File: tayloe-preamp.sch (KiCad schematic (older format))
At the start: 13 parts, among them J1 PCB_SMA_EDGE, J2 PCB_SMA_EDGE, J3 Conn_01x01_Female, Q1 2N2222, T1 T37_XFRM

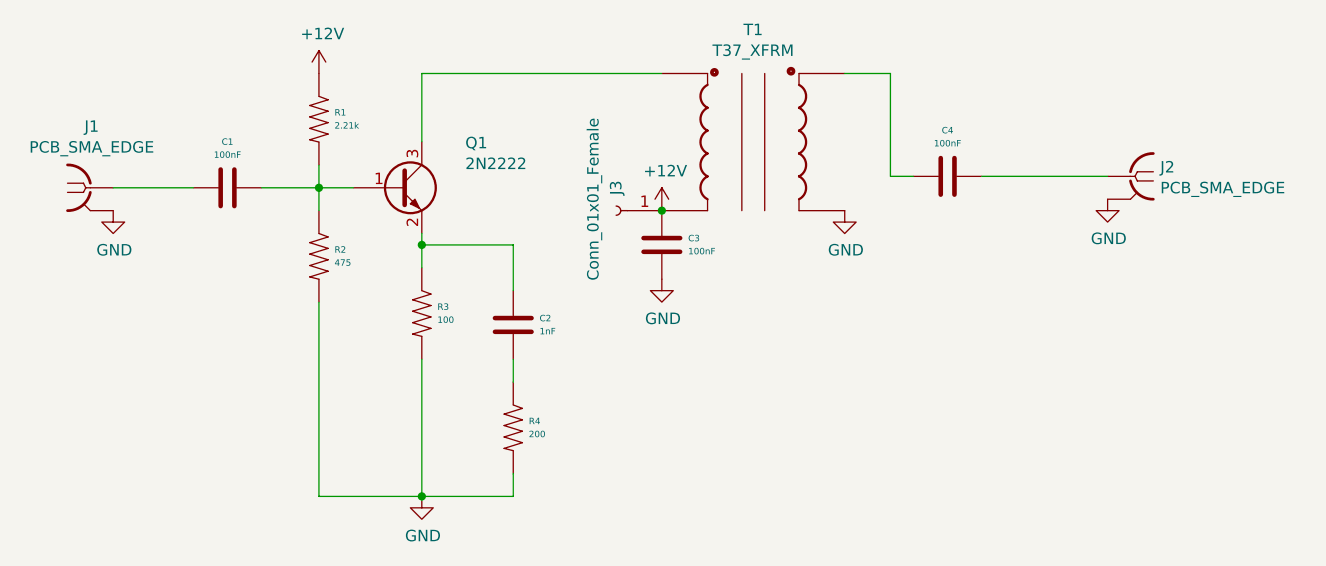
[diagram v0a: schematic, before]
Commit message: added 50 ohm input
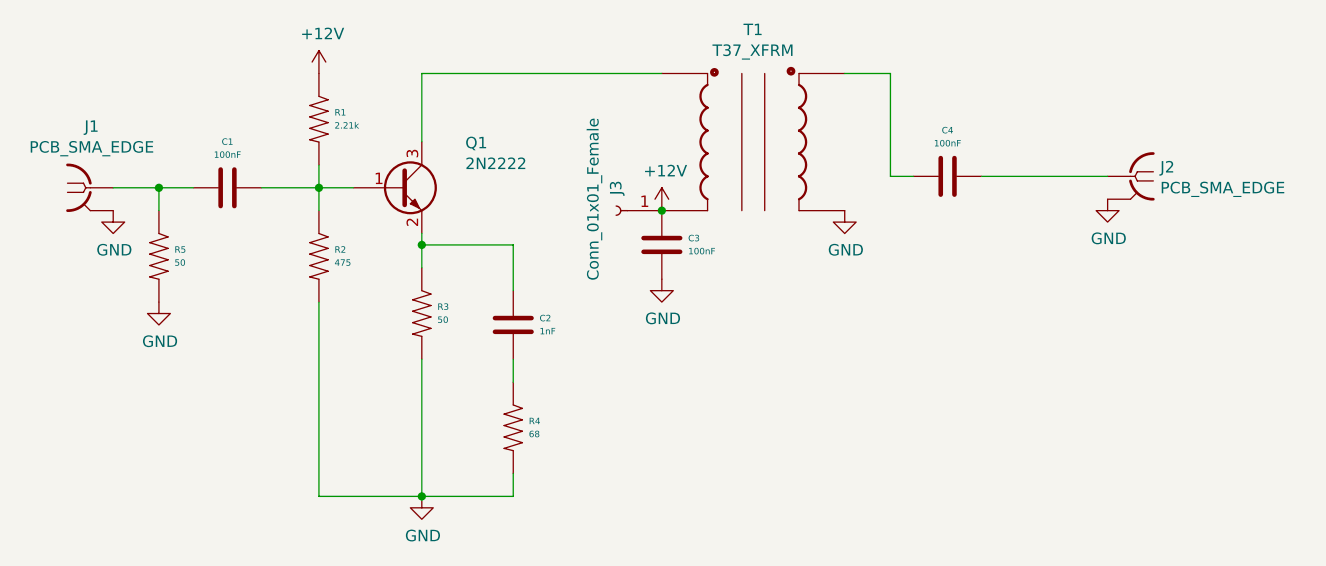
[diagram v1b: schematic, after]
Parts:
- added R5: 50, Xenir:Resistor 1206, symbol Xenir:Resistor
- R3: value 100 -> 50
- R4: value 200 -> 68
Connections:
- net GND: now also R5.2
- net at C1.2, J1.1: now also R5.1
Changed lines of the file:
@@
 P 4050 3750
 F 0 "R3" V 4021 3818 28  0000 L CNN
-F 1 "100" V 4078 3818 28  0000 L CNN
+F 1 "50" V 4078 3818 28  0000 L CNN
 F 2 "Xenir:Resistor 1206" H 4050 3650 50  0001 C CNN
 F 3 "" H 4050 3650 50  0001 C CNN
@@
 P 4450 4250
 F 0 "R4" V 4421 4318 28  0000 L CNN
-F 1 "200" V 4478 4318 28  0000 L CNN
+F 1 "68" V 4478 4318 28  0000 L CNN
 F 2 "Xenir:Resistor 1206" H 4450 4150 50  0001 C CNN
 F 3 "" H 4450 4150 50  0001 C CNN
@@
 $EndComp
 Wire Wire Line
-	2700 3200 3050 3200
+	2700 3200 2900 3200
 Wire Wire Line
 	3350 3200 3600 3200
@@
 	-1   0    0    1
 $EndComp
+$Comp
+L Xenir:Resistor R5
+U 1 1 639CE399
+P 2900 3500
+F 0 "R5" V 2871 3568 28  0000 L CNN
+F 1 "50" V 2928 3568 28  0000 L CNN
+F 2 "Xenir:Resistor 1206" H 2900 3400 50  0001 C CNN
+F 3 "" H 2900 3400 50  0001 C CNN
+	1    2900 3500
+	0    1    1    0
+$EndComp
+$Comp
+L power:GND #PWR0108
+U 1 1 639CEF49
+P 2900 3700
+F 0 "#PWR0108" H 2900 3450 50  0001 C CNN
+F 1 "GND" H 2905 3527 50  0000 C CNN
+F 2 "" H 2900 3700 50  0001 C CNN
+F 3 "" H 2900 3700 50  0001 C CNN
+	1    2900 3700
+	1    0    0    -1
+$EndComp
+Wire Wire Line
+	2900 3300 2900 3200
+Connection ~ 2900 3200
+Wire Wire Line
+	2900 3200 3050 3200
 $EndSCHEMATC

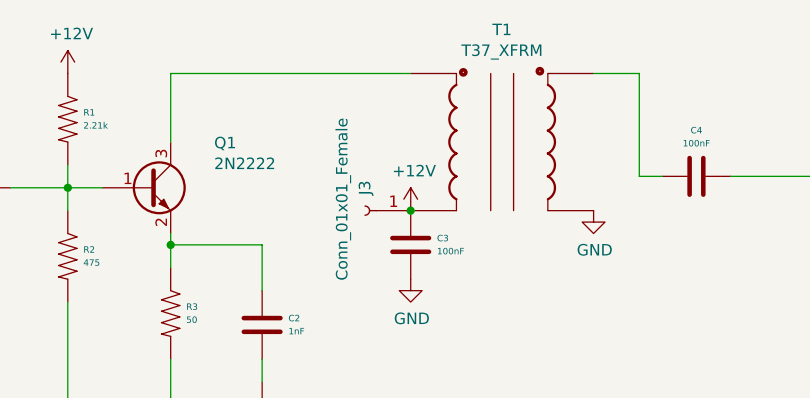
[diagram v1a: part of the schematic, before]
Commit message: changed to inductor
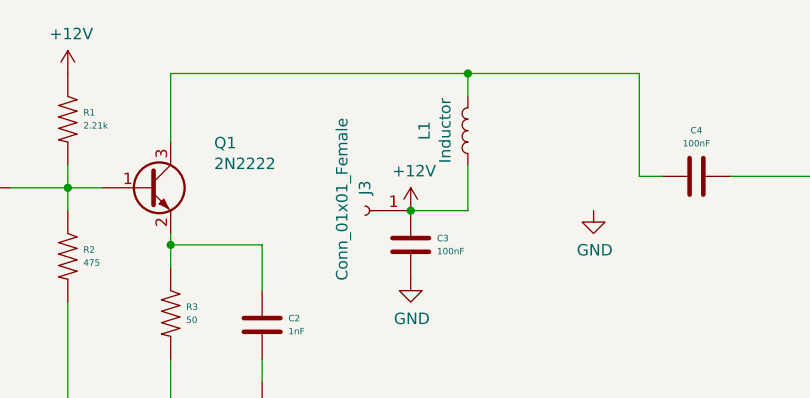
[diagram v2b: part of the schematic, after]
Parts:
- removed T1: T37_XFRM, Xenir:T37 Transformer, symbol Xenir:T37_XFRM
- added L1: Inductor, Xenir:T37_Inductor, symbol Xenir:Inductor
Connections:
- net +12V: now also L1.1
- net at Q1.3 (C): now also C4.2, L1.2
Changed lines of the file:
@@
-$EndComp
-$Comp
-L Xenir:T37_XFRM T1
-U 1 1 639E1E90
-P 5500 2550
-F 0 "T1" H 5500 2591 50  0000 C CNN
-F 1 "T37_XFRM" H 5500 2500 50  0000 C CNN
-F 2 "Xenir:T37 Transformer" H 5500 2550 50  0001 C CNN
-F 3 "" H 5500 2550 50  0001 C CNN
-	1    5500 2550
-	1    0    0    -1
 $EndComp
 $Comp
@@
 	1    0    0    -1
 $EndComp
-Wire Wire Line
-	5900 2700 6100 2700
-Wire Wire Line
-	4050 2700 5100 2700
 Wire Wire Line
 	4050 2700 4050 3000
@@
 Wire Wire Line
 	2900 3200 3050 3200
+$Comp
+L Xenir:Inductor L1
+U 1 1 639CFD79
+P 5350 2950
+F 0 "L1" H 5350 3140 50  0000 C CNN
+F 1 "Inductor" H 5350 3049 50  0000 C CNN
+F 2 "Xenir:T37_Inductor" H 5350 3050 50  0001 C CNN
+F 3 "" H 5350 3050 50  0001 C CNN
+	1    5350 2950
+	0    -1   -1   0
+$EndComp
+Wire Wire Line
+	5350 2700 5350 2800
+Wire Wire Line
+	5350 2700 6100 2700
+Wire Wire Line
+	5350 2700 4050 2700
+Connection ~ 5350 2700
+Wire Wire Line
+	5350 3100 5350 3300
+Wire Wire Line
+	5350 3300 5100 3300
 $EndSCHEMATC

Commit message: gg
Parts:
- L1: value Inductor -> T37-43 10T
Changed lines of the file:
@@
 P 5350 2950
 F 0 "L1" H 5350 3140 50  0000 C CNN
-F 1 "Inductor" H 5350 3049 50  0000 C CNN
+F 1 "T37-43 10T" H 5350 3049 50  0000 C CNN
 F 2 "Xenir:T37_Inductor" H 5350 3050 50  0001 C CNN
 F 3 "" H 5350 3050 50  0001 C CNN

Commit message: gg
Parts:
- C1, C2, C3, C4: symbol Xenir:Capacitor -> tayloe-preamp-rescue:Capacitor-Xenir
- J1, J2: symbol Xenir:PCB_SMA_EDGE -> tayloe-preamp-rescue:PCB_SMA_EDGE-Xenir
- L1: symbol Xenir:Inductor -> tayloe-preamp-rescue:Inductor-Xenir
- Q1: symbol Xenir:2N3904-SMD -> tayloe-preamp-rescue:2N3904-SMD-Xenir
- R1, R2, R3, R4, R5: symbol Xenir:Resistor -> tayloe-preamp-rescue:Resistor-Xenir
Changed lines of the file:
@@
 $EndDescr
 $Comp
-L Xenir:2N3904-SMD Q1
+L tayloe-preamp-rescue:2N3904-SMD-Xenir Q1
 U 1 1 639CC4F8
 P 4050 3050
@@
 $EndComp
 $Comp
-L Xenir:Resistor R1
+L tayloe-preamp-rescue:Resistor-Xenir R1
 U 1 1 639CCA36
 P 3600 2900
@@
 $EndComp
 $Comp
-L Xenir:Resistor R2
+L tayloe-preamp-rescue:Resistor-Xenir R2
 U 1 1 639CD051
 P 3600 3500
@@
 $EndComp
 $Comp
-L Xenir:Resistor R3
+L tayloe-preamp-rescue:Resistor-Xenir R3
 U 1 1 639CD583
 P 4050 3750
@@
 $EndComp
 $Comp
-L Xenir:Resistor R4
+L tayloe-preamp-rescue:Resistor-Xenir R4
 U 1 1 639CD8F7
 P 4450 4250
@@
 $EndComp
 $Comp
-L Xenir:Capacitor C2
+L tayloe-preamp-rescue:Capacitor-Xenir C2
 U 1 1 639CDDE4
 P 4450 3800
@@
 	3600 3200 3600 3100
 $Comp
-L Xenir:Capacitor C1
+L tayloe-preamp-rescue:Capacitor-Xenir C1
 U 1 1 639D36DD
 P 3200 3200
@@
 $EndComp
 $Comp
-L Xenir:PCB_SMA_EDGE J1
+L tayloe-preamp-rescue:PCB_SMA_EDGE-Xenir J1
 U 1 1 639D3F28
 P 2600 3000
@@
 $EndComp
 $Comp
-L Xenir:PCB_SMA_EDGE J2
+L tayloe-preamp-rescue:PCB_SMA_EDGE-Xenir J2
 U 1 1 639D45C6
 P 7150 2950
@@
 $EndComp
 $Comp
-L Xenir:Capacitor C4
+L tayloe-preamp-rescue:Capacitor-Xenir C4
 U 1 1 639FBD90
 P 6350 3150
@@
 	6500 3150 7050 3150
 $Comp
-L Xenir:Capacitor C3
+L tayloe-preamp-rescue:Capacitor-Xenir C3
 U 1 1 639FD1F1
 P 5100 3450
@@
 $EndComp
 $Comp
-L Xenir:Resistor R5
+L tayloe-preamp-rescue:Resistor-Xenir R5
 U 1 1 639CE399
 P 2900 3500
@@
 	2900 3200 3050 3200
 $Comp
-L Xenir:Inductor L1
+L tayloe-preamp-rescue:Inductor-Xenir L1
 U 1 1 639CFD79
 P 5350 2950
